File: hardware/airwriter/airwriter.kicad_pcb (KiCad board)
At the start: 2 copper layers, 32 x 54 mm, 41 parts, among them J1 USB-C 5V in, J2 Mini-DIN-8 to printer, J3 Bring-up USB/UART, SW1 SW_SPST_B3U-1000P, U1 ESP32-S3-WROOM-1-N8R2, U2 MAX3490ESA+, U3 MAX3232ESE+, U4 AP7361C-33E, U5 USBLC6-2SC6

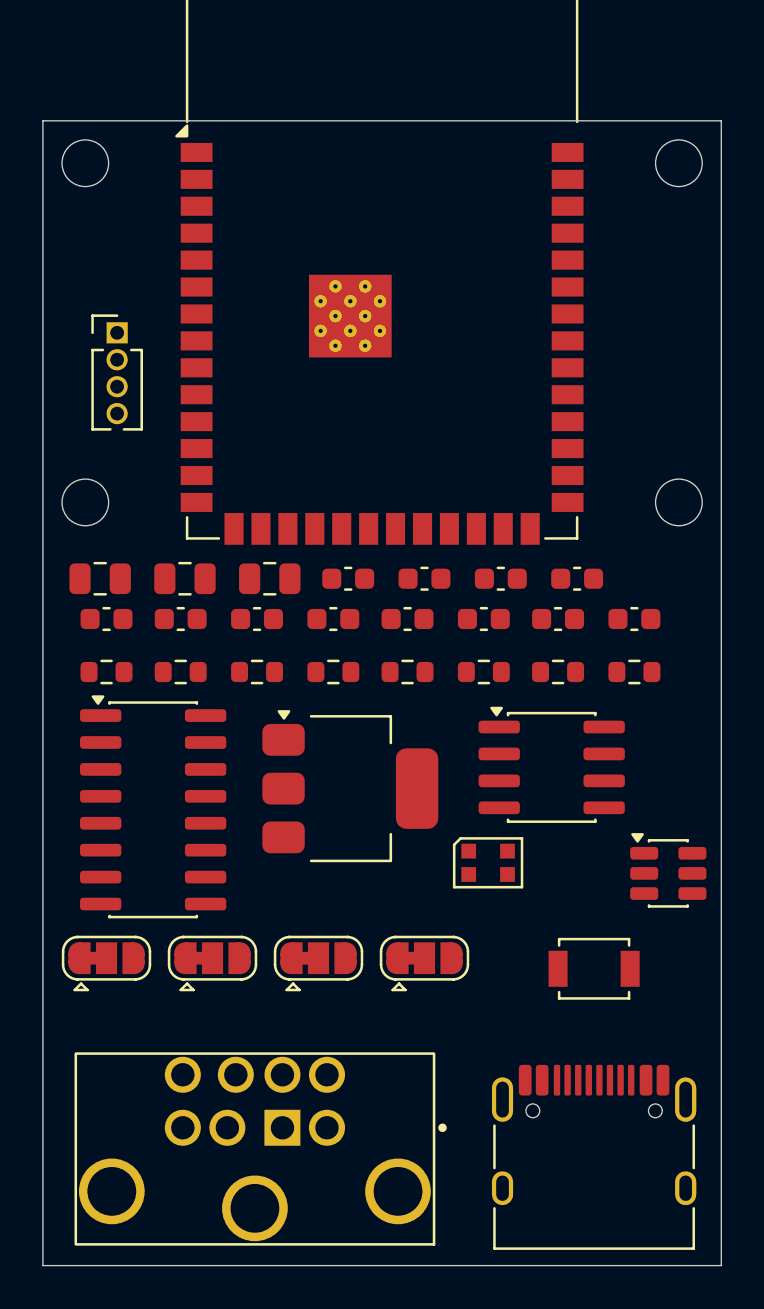
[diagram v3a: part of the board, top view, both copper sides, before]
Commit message: Ground plane, BOM with real DNP flags, fab exports, hardware README
- GND zone on B.Cu across the board.
- DNP is now a real symbol flag on R5/R6/R7/R9 rather than the word 'DNP' glued
  into the value string, so the BOM's DNP column is populated and an assembler
  will actually skip them. BOM is grouped by value+footprint+DNP, otherwise R8
  (populated 0R) and R9 (DNP 0R) merge into one misleading line.
- Exported BOM, pick-and-place, layer SVG, board stats, top render.
- README documents the size derivation, the 6 accepted DRC violations, the
  routing hand-off, and three MCP tool traps that corrupt this project.

Gerbers deliberately not exported: the board is not routed, so they would be
meaningless. 96 unconnected items remain.

Refs: W-568
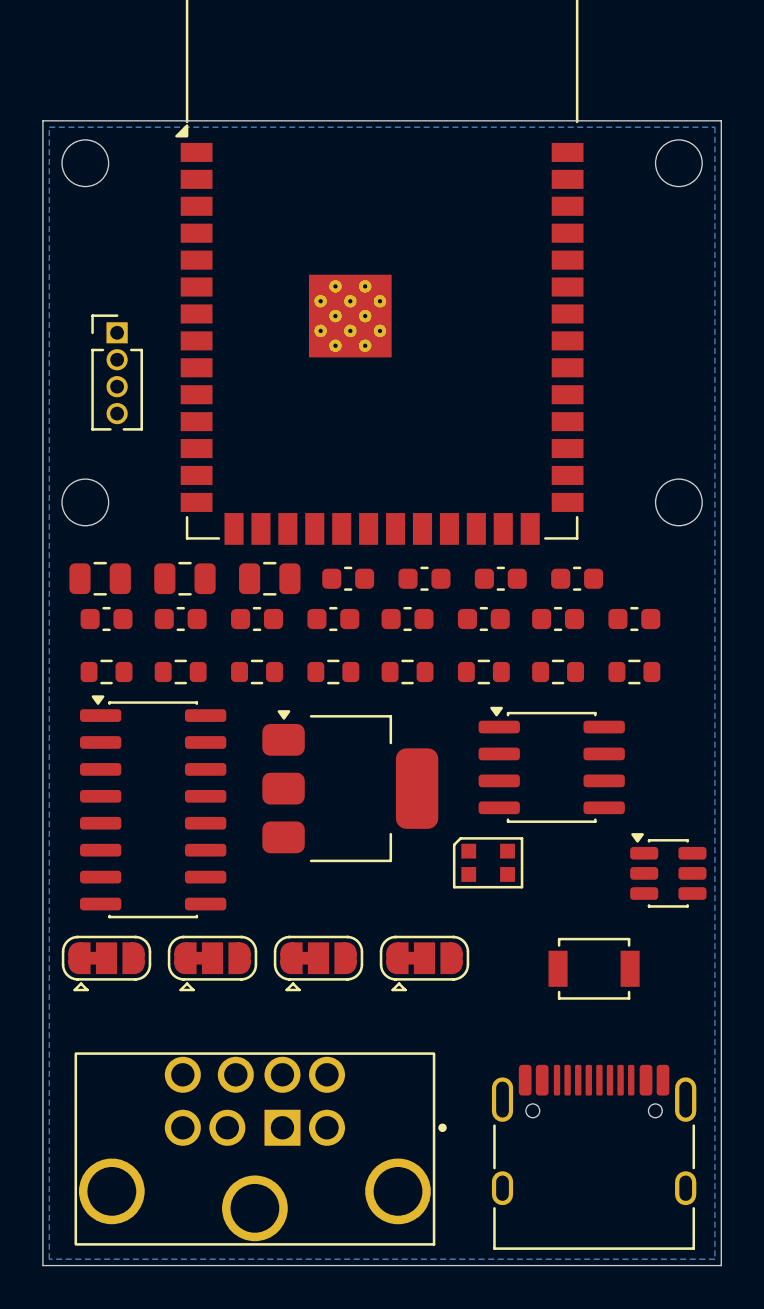
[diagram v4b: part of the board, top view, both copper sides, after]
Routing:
- added copper zone on B.Cu, net GND
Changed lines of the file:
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@@
 		)
 	)
-)
+  (zone (net 0) (net_name "GND") (layer "B.Cu")
+    (hatch edge 0.508)
+    (connect_pads (clearance 0.25))
+    (min_thickness 0.2)
+    (fill yes (thermal_gap 0.5) (thermal_bridge_width 0.5))
+    (polygon (pts
+      (xy 100.3 60.3)
+      (xy 131.7 60.3)
+      (xy 131.7 113.7)
+      (xy 100.3 113.7)
+    ))
+  ))

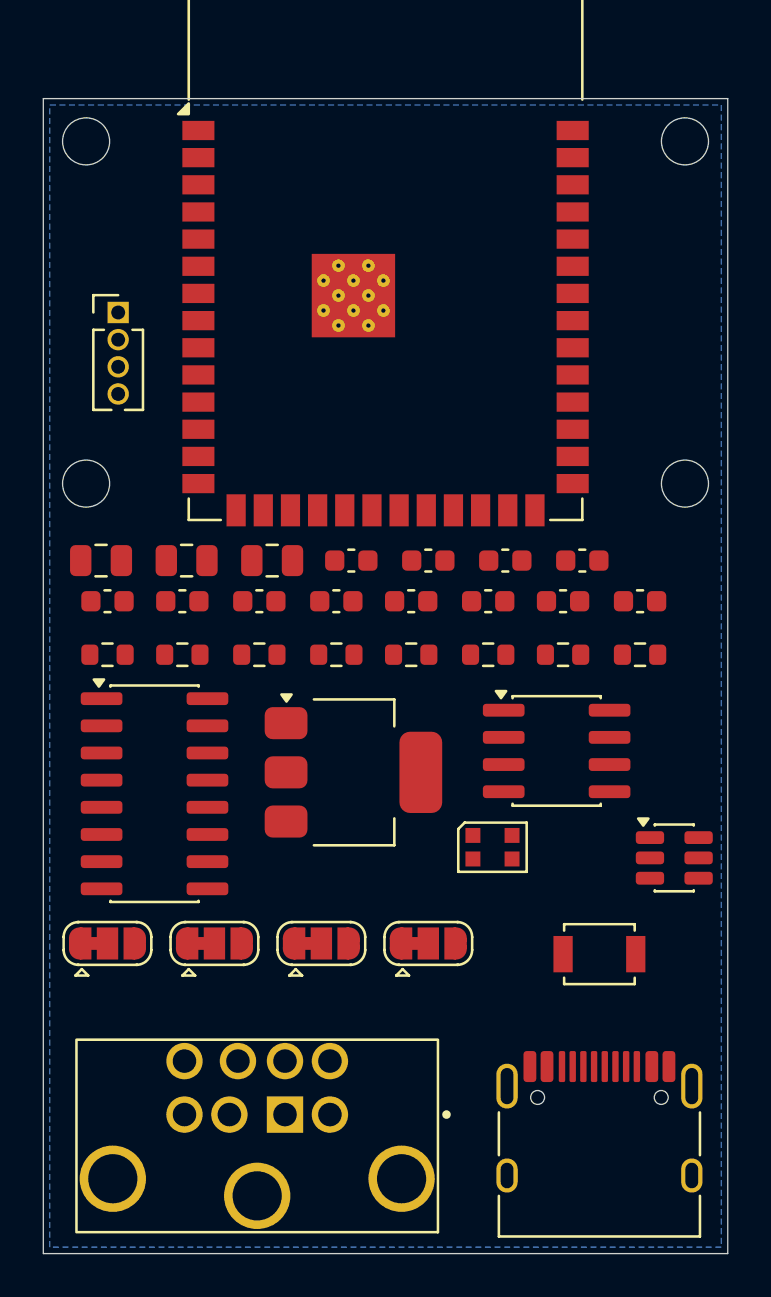
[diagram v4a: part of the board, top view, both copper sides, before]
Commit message: Route the board via Freerouting: 0 unconnected
571 segments across both layers, 58 vias at 0.6/0.3mm. Every net connected.

Committing the raw router output before cleanup so there is a restore point.

Refs: W-568
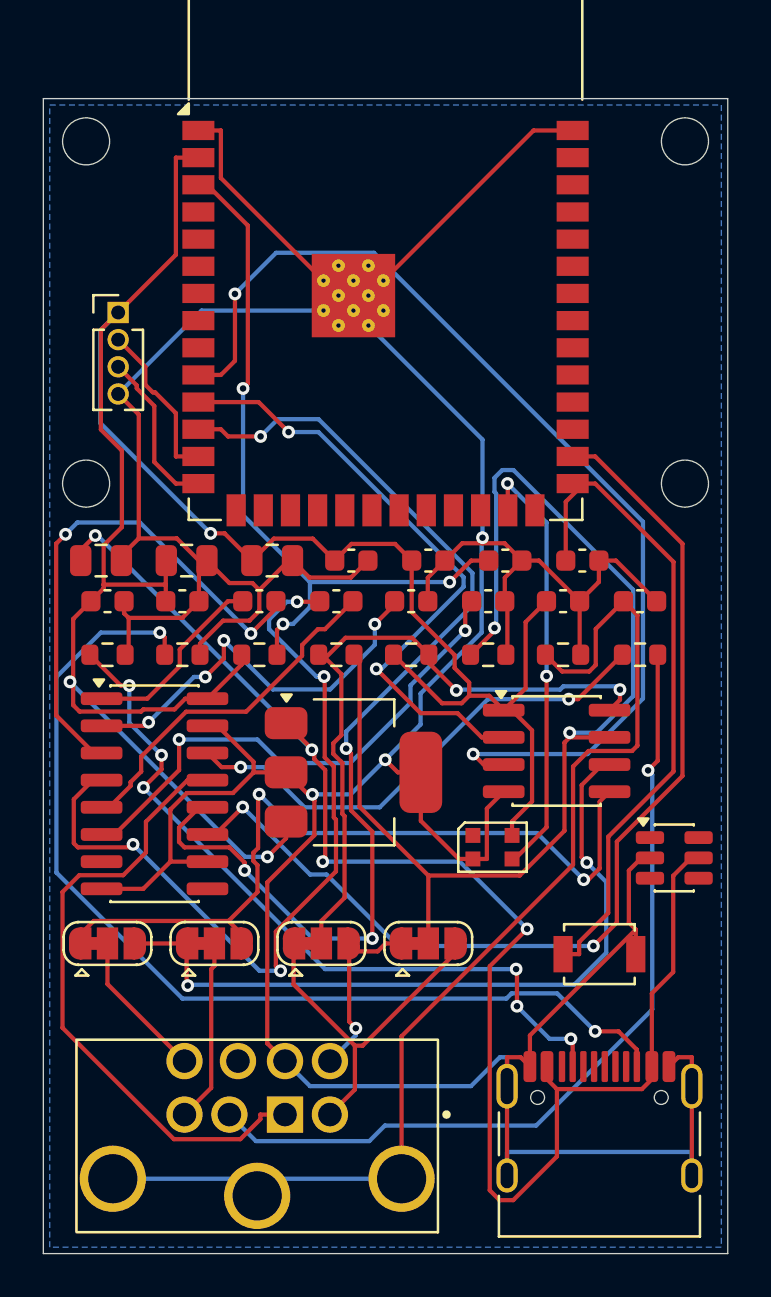
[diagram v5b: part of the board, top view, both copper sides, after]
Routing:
- net /GND: track 0.00 -> 225.9 mm, vias 0 -> 3
- net /+3V3: track 0.00 -> 109.4 mm, vias 0 -> 3
- net /VBUS: track 0.00 -> 71.5 mm, vias 0 -> 4
- net /RS422_B: track 0.00 -> 55.1 mm, vias 0 -> 2
- net /SHELL: track 0.00 -> 53.5 mm
- net /UART_CTS: track 0.00 -> 49.8 mm, vias 0 -> 4
- net /UART_TX: track 0.00 -> 49.1 mm, vias 0 -> 2
- net /HSKI_DRV: track 0.00 -> 48.6 mm, vias 0 -> 2
- net /CC2: track 0.00 -> 47.5 mm, vias 0 -> 2
- net /PR_HSKI: track 0.00 -> 39.7 mm, vias 0 -> 1
- net /CP2P: track 0.00 -> 37.9 mm, vias 0 -> 4
- net /RS422_Y: track 0.00 -> 37.2 mm, vias 0 -> 2
- net /CC1: track 0.00 -> 35.4 mm, vias 0 -> 6
- net /RS422_Z: track 0.00 -> 34.6 mm, vias 0 -> 2
- net /EN: track 0.00 -> 34.2 mm, vias 0 -> 3
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
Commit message: Clean up the routed board: DRC 278 -> 3, zero unconnected
The GND pour was never connected. add_zone created it on net "GND" while every
pad sits on "/GND" — KiCad's hierarchical name carries a leading slash. The
zone had been floating copper since it was added, and DRC surfaced this as 28
isolated-copper islands rather than as a disconnected zone.

Also fixed:
- Design rules had reverted to KiCad defaults when the project was reopened,
  putting min_through_hole_diameter back to 0.3mm and flagging the WROOM-1's
  0.2mm thermal vias. Re-applied.
- U1's antenna keepout polygon was stranded 46mm off the board. Footprint zones
  store absolute coordinates, so the scripted placement moved the pads but not
  the keepout, and DRC had never been enforcing it. Translated into place; it
  now sits at x92-140, y39-60, entirely in the overhang region above the board.
- H1/H2 moved 2.5mm clear of the corrected keepout.
- DNP set on the board footprints for R5/R6/R7/R9, not just the schematic, so
  the pick-and-place drops from 37 rows to the 33 parts actually populated.

Power traces left at 0.2mm. Widening to 0.4mm cost 55 clearance violations in
the routed density, and the width is not needed: IPC-2221 gives 0.74A at a 10C
rise on 1oz external copper, against a 500mA peak.

Exported gerbers, Excellon drill + map, BOM, pick-and-place and render.

Refs: W-568
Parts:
- moved H1 2.50 mm to (102.0, 64.5)
- moved H2 2.50 mm to (130.0, 64.5)
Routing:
- added copper zone on B.Cu, net /GND
- removed copper zone on B.Cu, net GND

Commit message: Remove the polarity jumpers and fix the receiver mapping
Two changes that belong together.

Receiver polarity was inverted. Apple's convention is that a binary 1 has TxD-
more negative than TxD+, so the + line is non-inverting. The MAX3490 needs
A > B at mark, which means A<-TxD+ (pin 6) and B<-TxD- (pin 3). The spec had
these swapped, so every received byte would have arrived inverted.

JP1-JP4 deleted. They existed as insurance against exactly the polarity question
above, but the ESP32 UART already provides it: uart_set_line_inverse() with
UART_SIGNAL_TXD_INV / UART_SIGNAL_RXD_INV. Inverting DI flips Y and Z together,
which is electrically identical to swapping the differential pair, and the same
holds for RO on the receive side. So polarity is now a one-line firmware change
rather than four parts and eight pads. The insurance survives; the components
do not.

U2 now drives and receives J2 directly. R5/R6/R7 (all DNP) move onto the
corrected nets, and the bias already pulled the right way: R6 holds TxD+ high
and R7 holds TxD- low, which is mark.

Board: jumper footprints removed, all 571 segments and 58 vias ripped up, pad
nets remapped. 37 footprints, schematic parity clean apart from J2's
deliberately unconnected GPi pin and the four mounting holes, which are
mechanical and not in the schematic.

Needs one more Freerouting pass. Fab outputs are stale until then.

Refs: W-568, W-564
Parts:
- removed JP1: RxD+ pol, Jumper:SolderJumper-3_P1.3mm_Bridged12_RoundedPad1.0x1.5mm
- removed JP2: RxD- pol, Jumper:SolderJumper-3_P1.3mm_Bridged12_RoundedPad1.0x1.5mm
- removed JP3: TxD- pol, Jumper:SolderJumper-3_P1.3mm_Bridged12_RoundedPad1.0x1.5mm
- removed JP4: TxD+ pol, Jumper:SolderJumper-3_P1.3mm_Bridged12_RoundedPad1.0x1.5mm
- R5: value 120R DNP -> 120R
- R6, R7: value 4.7k DNP -> 4.7k
- R9: value 0R DNP -> 0R
- SW1: value SW_SPST_B3U-1000P -> CONFIG/BOOT
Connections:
- R5 pad 1: /RS422_A -> /PR_TXD_P
- R5 pad 2: /RS422_B -> /PR_TXD_N
- R6 pad 2: /RS422_A -> /PR_TXD_P
- R7 pad 1: /RS422_B -> /PR_TXD_N
- U2 pad 5: /RS422_Y -> /PR_RXD_P
- U2 pad 6: /RS422_Z -> /PR_RXD_N
- U2 pad 7: /RS422_B -> /PR_TXD_N
- U2 pad 8: /RS422_A -> /PR_TXD_P
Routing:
- net /GND: track 225.9 -> 0.00 mm, vias 3 -> 0
- net /+3V3: track 109.4 -> 0.00 mm, vias 3 -> 0
- net /VBUS: track 71.5 -> 0.00 mm, vias 4 -> 0
- net /RS422_B: track 55.1 -> 0.00 mm, vias 2 -> 0
- net /SHELL: track 53.5 -> 0.00 mm
- net /UART_CTS: track 49.8 -> 0.00 mm, vias 4 -> 0
- net /UART_TX: track 49.1 -> 0.00 mm, vias 2 -> 0
- net /HSKI_DRV: track 48.6 -> 0.00 mm, vias 2 -> 0
- net /CC2: track 47.5 -> 0.00 mm, vias 2 -> 0
- net /PR_HSKI: track 39.7 -> 0.00 mm, vias 1 -> 0
- net /CP2P: track 37.9 -> 0.00 mm, vias 4 -> 0
- net /RS422_Y: track 37.2 -> 0.00 mm, vias 2 -> 0
- net /CC1: track 35.4 -> 0.00 mm, vias 6 -> 0
- net /RS422_Z: track 34.6 -> 0.00 mm, vias 2 -> 0
- net /EN: track 34.2 -> 0.00 mm, vias 3 -> 0
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
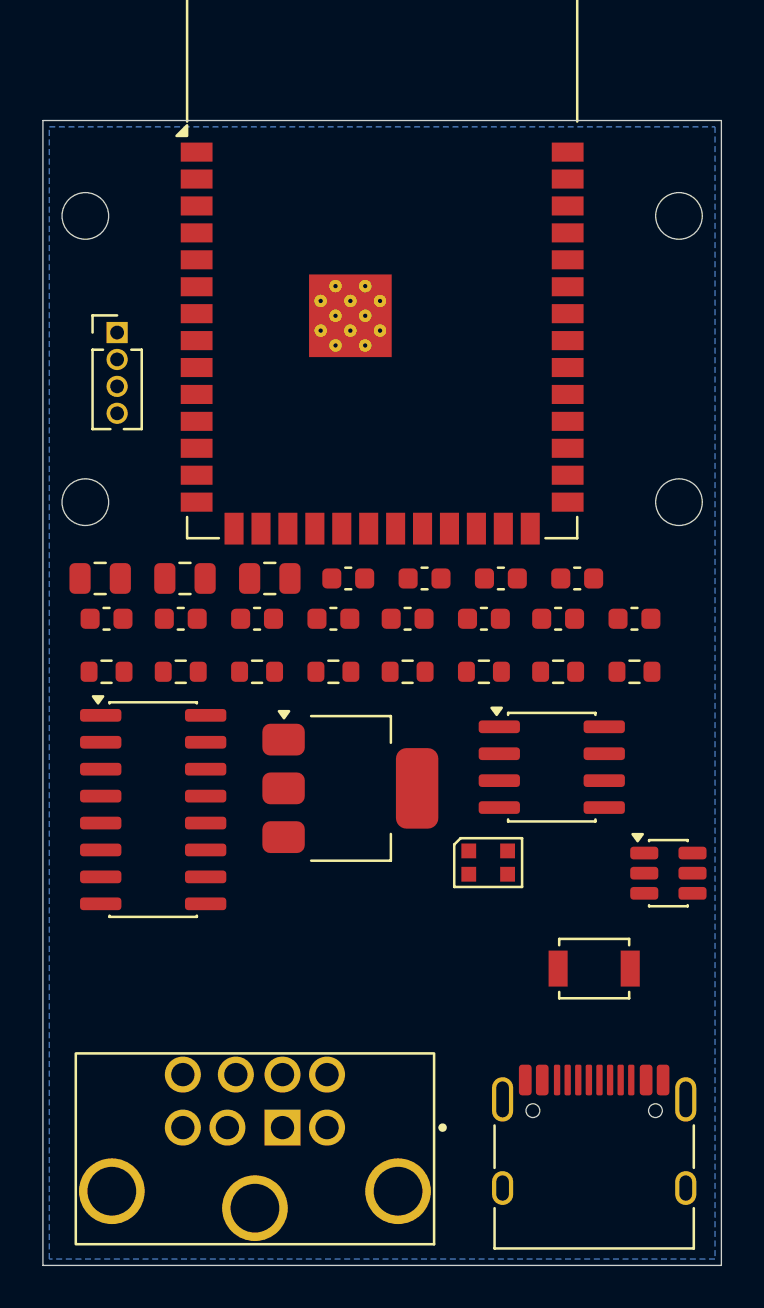
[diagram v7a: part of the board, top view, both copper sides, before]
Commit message: Re-route after jumper removal: 470 segments, 64 vias
Restore point before stitching-via cleanup. 7 GND connections still open and
one via too close to the board edge.

Refs: W-568
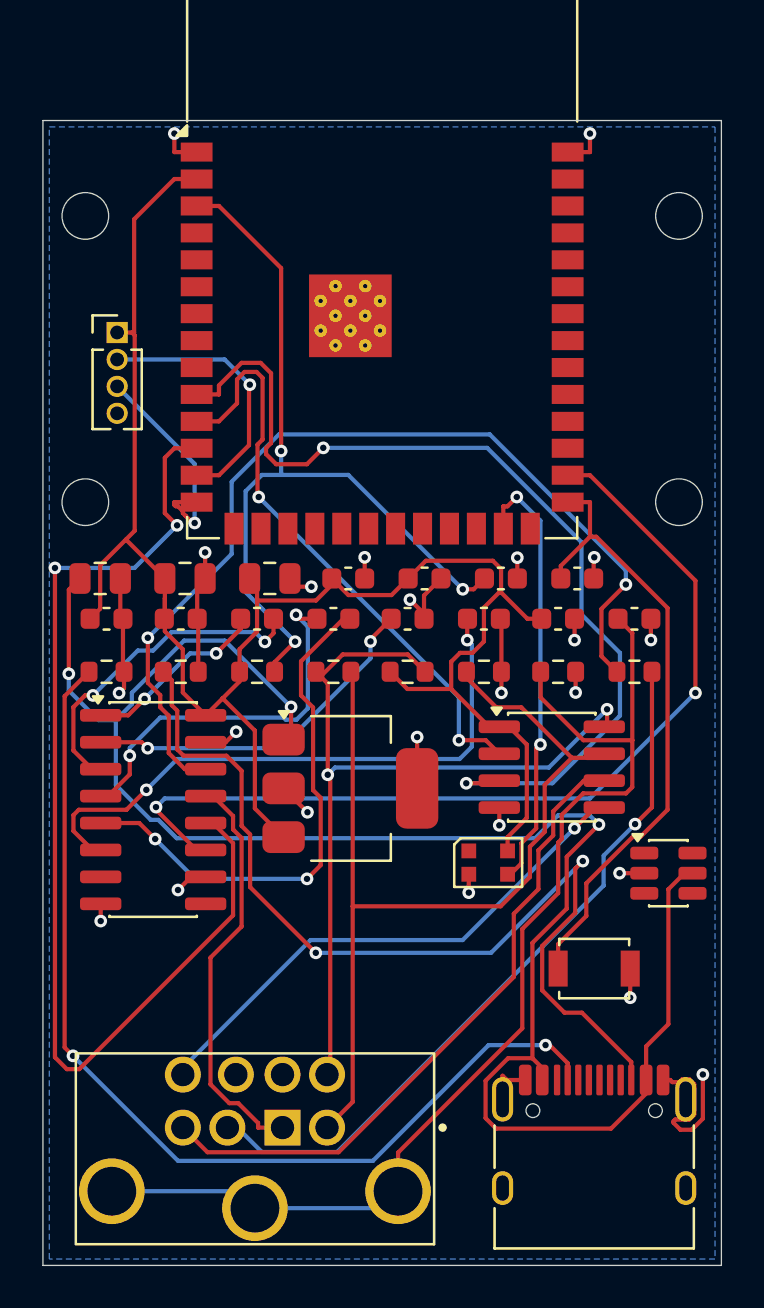
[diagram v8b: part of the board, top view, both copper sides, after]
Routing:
- net /VBUS: track 0.00 -> 86.9 mm, vias 0 -> 3
- net /+3V3: track 0.00 -> 86.4 mm
- net /SHELL: track 0.00 -> 53.6 mm
- net /GND: track 0.00 -> 52.6 mm, vias 0 -> 23
- net /UART_CTS: track 0.00 -> 51.5 mm, vias 0 -> 2
- net /CC1: track 0.00 -> 47.5 mm, vias 0 -> 2
- net /PR_TXD_N: track 0.00 -> 45.8 mm
- net /CC2: track 0.00 -> 45.1 mm, vias 0 -> 2
- net /UART_TX: track 0.00 -> 44.8 mm, vias 0 -> 2
- net /HSKI_RS232: track 0.00 -> 44.6 mm, vias 0 -> 2
- net /HSKI_DRV: track 0.00 -> 44.3 mm, vias 0 -> 2
- net /PR_TXD_P: track 0.00 -> 40.4 mm, vias 0 -> 2
- net /EN: track 0.00 -> 38.9 mm, vias 0 -> 3
- net /PR_HSKI: track 0.00 -> 34.5 mm, vias 0 -> 1
- net /PR_RXD_N: track 0.00 -> 31.1 mm
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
